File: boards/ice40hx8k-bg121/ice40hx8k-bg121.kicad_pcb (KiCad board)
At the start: 4 copper layers, 22.9 x 48.3 mm, 51 parts, among them J1 BANK 0, J2 BANK 1, J3 BANK 2, J4 BANK 3, U1 AP7361C-33Y5-13, U2 AP7361C-12Y5-13, U3 iCE40HX8K-BG121(121-Ball_caBG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, U4 LE25U20AMB, U5 ASDMB-xxxMHz

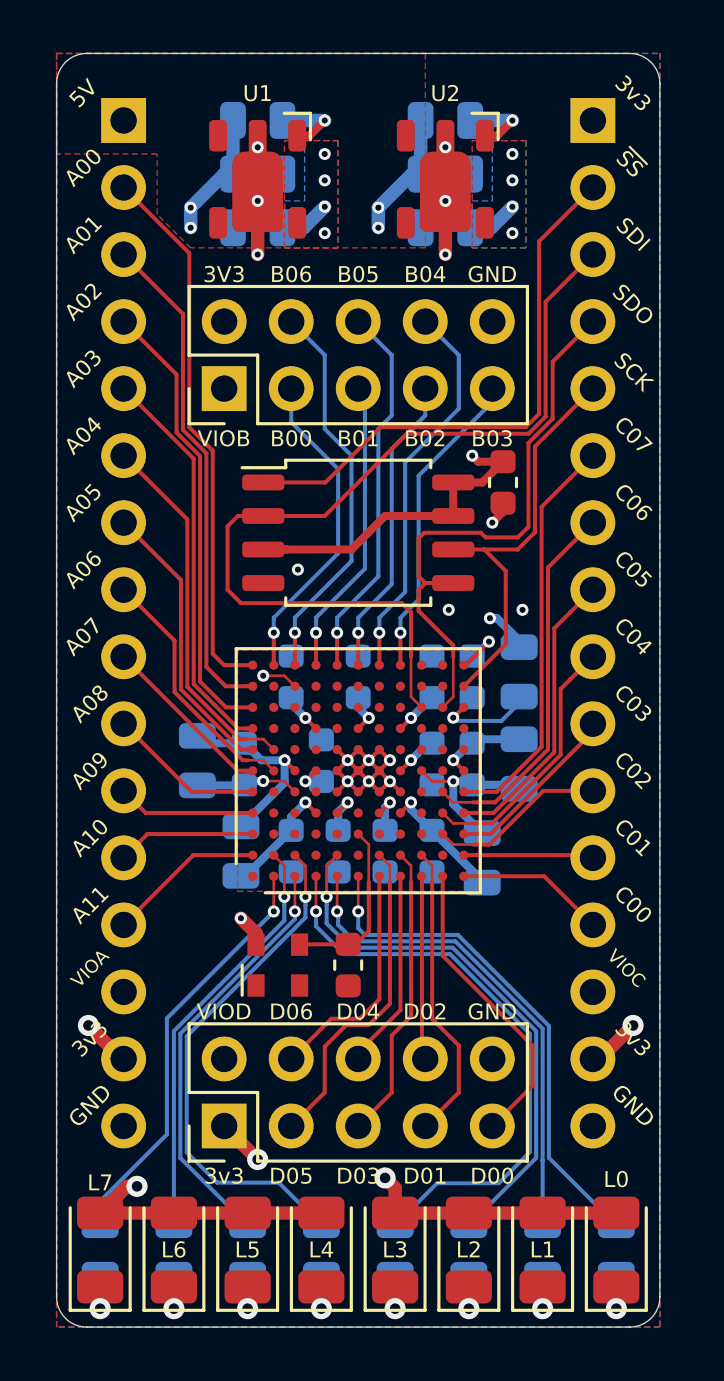
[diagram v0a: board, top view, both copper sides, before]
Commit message: Fixed errors in main README. Added boards.
Accidentally committed changes to ice40hx8k-bg121 and atsamd21e18a
boards.

The ice40hx8k-bg121 changes include adding access to CBSEL0/1 and
rerouting IO.

The atsamd21e18a changes include rerouting IO to prioritize USB
D+/- routing.
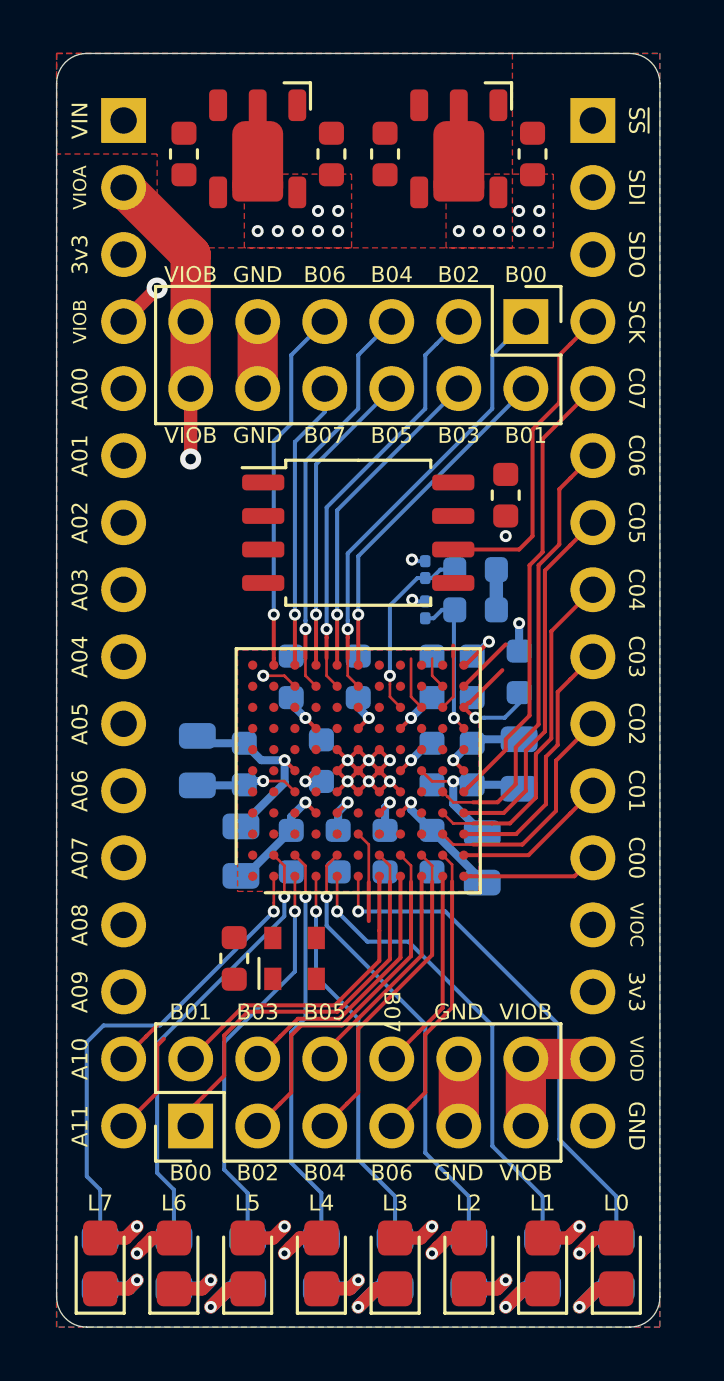
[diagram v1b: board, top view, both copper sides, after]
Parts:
- removed C20: 22p, Capacitor_SMD:C_0603_1608Metric
- removed REF**: OSHW-Symbol_6.7x6mm_SilkScreen, Symbol:OSHW-Symbol_6.7x6mm_SilkScreen
- added C21: 0.1u, Capacitor_SMD:C_0603_1608Metric, F.Cu at (27.1, 49.5)
- added JP1: CBSEL1, Resistor_SMD:R_0201_0603Metric, B.Cu at (34.3, 36.3)
- added JP2: CBSEL0, Resistor_SMD:R_0201_0603Metric, B.Cu at (34.3, 34.8)
- C1, C2, C3, C4: footprint Capacitor_SMD:C_0805_2012Metric -> Capacitor_SMD:C_0603_1608Metric; moved to F.Cu
- D10, D3, D4, D5, D6, D7, D8, D9: footprint LED_SMD:LED_1206_3216Metric -> LED_SMD:LED_0805_2012Metric_Castellated
- J1: value BANK 0 -> Conn_01x16
- J2: value BANK 1 -> Conn_01x16
- J3: value BANK 2 -> Conn_02x06_Odd_Even; footprint Connector_PinHeader_2.54mm:PinHeader_2x05_P2.54mm_Vertical -> Connector_PinHeader_2.54mm:PinHeader_2x06_P2.54mm_Vertical
- J4: value BANK 3 -> Conn_02x06_Odd_Even; footprint Connector_PinHeader_2.54mm:PinHeader_2x05_P2.54mm_Vertical -> Connector_PinHeader_2.54mm:PinHeader_2x06_P2.54mm_Vertical
- R1, R12, R2: footprint Resistor_SMD:R_0805_2012Metric -> Resistor_SMD:R_0603_1608Metric
- moved R1 20.3 mm to (36.2, 36.3)
- moved R2 17.1 mm to (36.2, 34.8)
- moved J4 11.7 mm to (38.1, 25.4), turned to 270 degrees
- moved C4 4.33 mm to (38.4, 19.1), turned to 90 degrees
- moved C2 3.95 mm to (30.7, 19.1), turned to 90 degrees
- moved C1 2.90 mm to (25.1, 19.1), turned to 90 degrees
- moved C3 2.41 mm to (32.8, 19.1), turned to 90 degrees
- moved J3 1.27 mm to (25.4, 55.9)
- moved U2 1.26 mm to (35.6, 18.9)
- moved U1 1.15 mm to (27.9, 18.9)
- moved U5 0.68 mm to (29.3, 49.5)
- moved D10 0.51 mm to (41.5, 61.1)
- moved D3 0.51 mm to (22.0, 61.1)
- moved D4 0.51 mm to (24.8, 61.1)
- moved D5 0.51 mm to (27.6, 61.1)
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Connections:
- net Net-(U3-PadK8) renamed CDONE
- C19 pad 2: VCCIO_C -> +3V3
- J1 pad 10: IO_A08 -> IO_A05
- J1 pad 11: IO_A09 -> IO_A06
- J1 pad 12: IO_A10 -> IO_A07
- J1 pad 13: IO_A11 -> IO_A08
- J1 pad 14: VCCIO_A -> IO_A09
- J1 pad 15: +3V3 -> IO_A10
- J1 pad 16: GND -> IO_A11
- J1 pad 2: IO_A00 -> VCCIO_B
- J1 pad 3: IO_A01 -> +3V3
- J1 pad 4: IO_A02 -> VCCIO_A
- J1 pad 5: IO_A03 -> IO_A00
- J1 pad 6: IO_A04 -> IO_A01
- J1 pad 7: IO_A05 -> IO_A02
- J1 pad 8: IO_A06 -> IO_A03
- J1 pad 9: IO_A07 -> IO_A04
- J2 pad 1: +3V3 -> PROG_SS_B
- J2 pad 10: IO_C03 -> IO_C02
- J2 pad 11: IO_C02 -> IO_C01
- J2 pad 12: IO_C01 -> IO_C00
- J2 pad 13: IO_C00 -> VCCIO_C
- J2 pad 14: VCCIO_C -> +3V3
- J2 pad 15: +3V3 -> VCCIO_D
- J2 pad 2: PROG_SS_B -> PROG_SDI
- J2 pad 3: PROG_SDI -> PROG_SDO
- J2 pad 4: PROG_SDO -> PROG_SCK
- J2 pad 5: PROG_SCK -> IO_C07
- J2 pad 6: IO_C07 -> IO_C06
- J2 pad 7: IO_C06 -> IO_C05
- J2 pad 8: IO_C05 -> IO_C04
- J2 pad 9: IO_C04 -> IO_C03
- J3 pad 1: +3V3 -> IO_D00
- J3 pad 2: VCCIO_D -> IO_D01
- J3 pad 3: IO_D05 -> IO_D02
- J3 pad 4: IO_D06 -> IO_D03
- J3 pad 5: IO_D03 -> IO_D04
- J3 pad 6: IO_D04 -> IO_D05
- J3 pad 7: IO_D01 -> IO_D06
- J3 pad 8: IO_D02 -> IO_D07
- J3 pad 9: IO_D00 -> GND
- J4 pad 1: VCCIO_B -> IO_B00
- J4 pad 2: +3V3 -> IO_B01
- J4 pad 3: IO_B00 -> IO_B02
- J4 pad 4: IO_B06 -> IO_B03
- J4 pad 5: IO_B01 -> IO_B04
- J4 pad 7: IO_B02 -> IO_B06
- J4 pad 8: IO_B04 -> IO_B07
- J4 pad 9: IO_B03 -> GND
- R1 pad 1: +5V -> CBSEL0
- R1 pad 2: Net-(R1-Pad2) -> GND
- R2 pad 1: +5V -> CBSEL1
- R2 pad 2: Net-(R2-Pad2) -> GND
- U1 pad 1: Net-(R1-Pad2) -> +5V
- U2 pad 1: Net-(R2-Pad2) -> +5V
- U3 pad A2: IO_A11 -> Net-(U3-PadA2)
- U3 pad A3: IO_A10 -> Net-(U3-PadA3)
- U3 pad A4: IO_A09 -> IO_A10
- U3 pad B11: IO_B00 -> IO_B06
- U3 pad B4: Net-(U3-PadB4) -> IO_A11
- U3 pad B5: Net-(U3-PadB5) -> IO_A09
- U3 pad C11: IO_B06 -> IO_B07
- U3 pad D10: Net-(U3-PadD10) -> IO_B04
- U3 pad D11: IO_B01 -> IO_B05
- U3 pad E10: Net-(U3-PadE10) -> IO_B02
- U3 pad E11: IO_B05 -> IO_B03
- U3 pad F10: Net-(U3-PadF10) -> IO_B00
- U3 pad F11: IO_B02 -> IO_B01
- U3 pad G1: IO_D06 -> IO_D01
- U3 pad G11: IO_B04 -> Net-(U3-PadG11)
- U3 pad G2: IO_D05 -> IO_D00
- U3 pad H1: IO_D04 -> IO_D03
- U3 pad H11: IO_B03 -> Net-(U3-PadH11)
- U3 pad H2: IO_D03 -> IO_D02
- U3 pad J1: IO_D02 -> IO_D05
- U3 pad J2: IO_D01 -> IO_D04
- U3 pad K1: IO_D00 -> IO_D07
- U3 pad K10: Net-(U3-PadK10) -> PROG_SS_B
- U3 pad K2: Net-(U3-PadK2) -> IO_D06
- U4 pad 3: VCCIO_C -> +3V3
- U4 pad 7: VCCIO_C -> +3V3
- U4 pad 8: VCCIO_C -> +3V3
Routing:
- net PROG_SDI: track 34.1 -> 2.01 mm
- net VCCIO_C: track 42.6 -> 19.4 mm, vias 3 -> 2
- net IO_A00: track 20.8 -> 0.00 mm
- net PROG_SS_B: track 21.0 -> 1.21 mm
- net PROG_SDO: track 21.7 -> 2.51 mm
- net IO_A01: track 19.0 -> 0.00 mm
- net IO_A02: track 17.2 -> 0.00 mm
- net IO_A03: track 15.2 -> 0.10 mm
- net IO_A04: track 14.0 -> 0.00 mm
- net VCCIO_A: track 12.3 -> 25.4 mm, vias 1 -> 2
- net IO_B07: track 0.00 -> 10.9 mm, vias 0 -> 1
- net IO_A05: track 10.9 -> 0.00 mm
- net +5V: track 9.85 -> 0.00 mm, vias 4 -> 0
- net IO_A06: track 9.77 -> 0.00 mm
- net VCCIO_B: track 19.2 -> 28.4 mm, vias 1 -> 2
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- removed copper zone on B.Cu, net +1V2
- removed copper zone on B.Cu, net +3V3
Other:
- board text added: "B07"
- board text added: "CBSEL0"
- board text added: "CBSEL1"
- board text added: "VIN"
- board text removed: "3V3"
- board text removed: "5V"
- board text removed: "D00"
- board text removed: "D01"
- board text removed: "D02"
- board text removed: "D03"
- board text removed: "D04"
- board text removed: "D05"
- board text removed: "D06"

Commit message: Added FT2232H breakout for programming /boards/ice40hx8k-bg121/
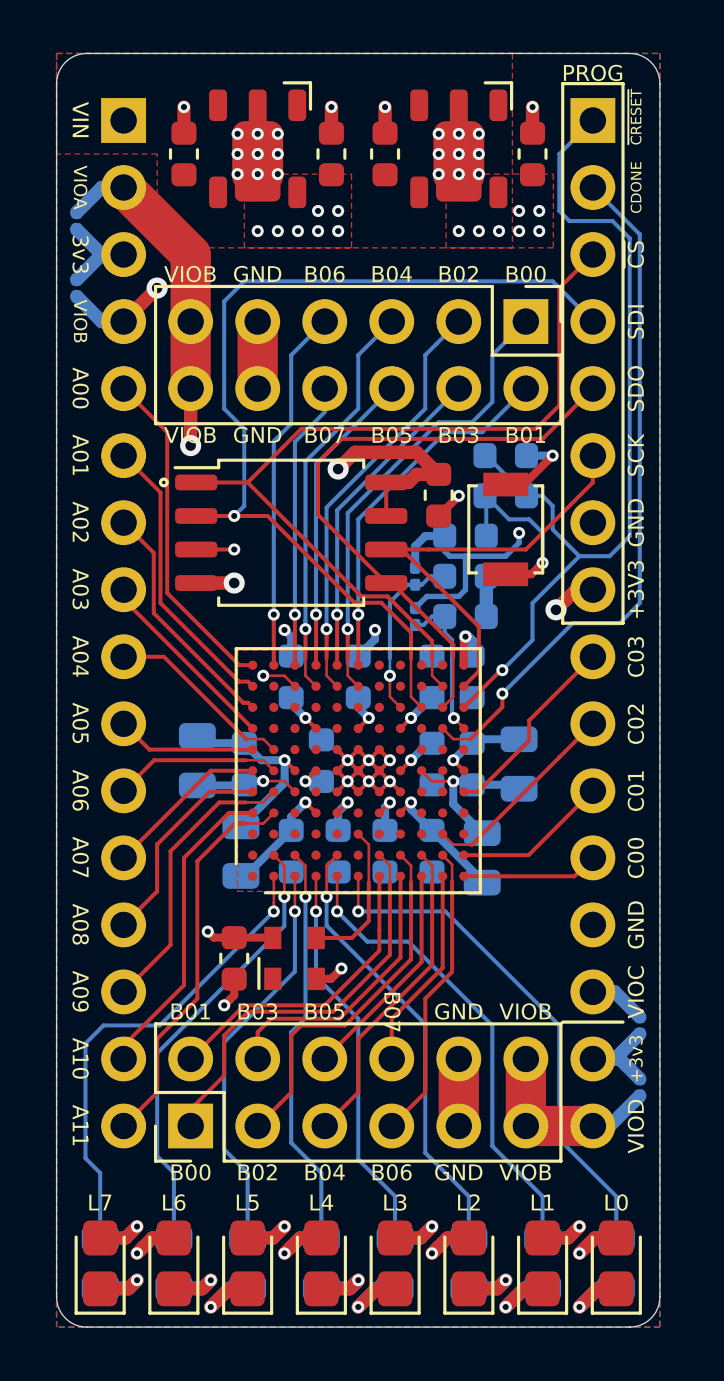
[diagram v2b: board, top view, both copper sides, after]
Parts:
- added C20: 0.1u, Capacitor_SMD:C_0603_1608Metric, B.Cu at (37.3, 30.5)
- added JP3: VCCIO_A, jkiv-library:J_NO_0201_0603Metric, B.Cu at (21.1, 24.1)
- added JP4: VCCIO_B, jkiv-library:J_NO_0201_0603Metric, B.Cu at (21.1, 21.6)
- added JP5: VCCIO_C, jkiv-library:J_NO_0201_0603Metric, B.Cu at (42.4, 52.1)
- added JP6: VCCIO_D, jkiv-library:J_NO_0201_0603Metric, B.Cu at (42.4, 54.4)
- added R14: 10k, Resistor_SMD:R_0603_1608Metric, B.Cu at (35.8, 33.5)
- added REF**: OSHW-Symbol_6.7x6mm_SilkScreen, Symbol:OSHW-Symbol_6.7x6mm_SilkScreen, B.Cu at (32.0, 19.8)
- added SW1: B3U-1000P, Button_Switch_SMD:SW_SPST_B3U-1000P, F.Cu at (37.3, 33.3)
- JP1, JP2: footprint Resistor_SMD:R_0201_0603Metric -> jkiv-library:J_NO_0201_0603Metric
- moved R12 6.69 mm to (37.3, 32.0), turned to 0 degrees
- moved C19 2.54 mm to (34.8, 32.0)
- moved U4 2.54 mm to (29.2, 33.4)
- moved JP1 0.46 mm to (33.9, 36.6)
- moved JP2 0.46 mm to (33.9, 35.1)
- moved R1 0.46 mm to (35.8, 36.6)
- moved R2 0.46 mm to (35.8, 35.1)
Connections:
- J2 pad 1: PROG_SS_B -> PROG_CRESET_B
- J2 pad 13: VCCIO_C -> GND
- J2 pad 14: +3V3 -> VCCIO_C
- J2 pad 15: VCCIO_D -> +3V3
- J2 pad 16: GND -> VCCIO_D
- J2 pad 2: PROG_SDI -> CDONE
- J2 pad 3: PROG_SDO -> PROG_SS_B
- J2 pad 4: PROG_SCK -> PROG_SDI
- J2 pad 5: IO_C07 -> PROG_SDO
- J2 pad 6: IO_C06 -> PROG_SCK
- J2 pad 7: IO_C05 -> GND
- J2 pad 8: IO_C04 -> +3V3
- R12 pad 1: VCCIO_C -> Net-(R12-Pad1)
- U3 pad K4: IO_C04 -> Net-(U3-PadK4)
- U3 pad K5: IO_C06 -> Net-(U3-PadK5)
- U3 pad L3: IO_C03 -> Net-(U3-PadL3)
- U3 pad L4: IO_C05 -> Net-(U3-PadL4)
- U3 pad L5: IO_C07 -> IO_C03
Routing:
- net PROG_SDI: track 2.01 -> 36.5 mm, vias 0 -> 1
- net PROG_SS_B: track 1.21 -> 32.6 mm
- net PROG_CRESET_B: track 4.90 -> 33.8 mm
- net CDONE: track 0.00 -> 26.6 mm, vias 0 -> 1
- net +3V3: track 25.7 -> 47.1 mm, vias 19 -> 22
- net PROG_SDO: track 2.51 -> 23.3 mm
- net GND: track 18.5 -> 36.2 mm, vias 7 -> 35
- net IO_C07: track 17.3 -> 0.00 mm
- net IO_C06: track 16.9 -> 0.00 mm
- net IO_C05: track 13.9 -> 0.00 mm
- net IO_C04: track 12.9 -> 0.00 mm
- net IO_A00: track 0.00 -> 12.8 mm
- net IO_A01: track 0.00 -> 11.0 mm
- net IO_A09: track 0.00 -> 10.9 mm
- net IO_A11: track 3.93 -> 14.8 mm
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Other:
- board text added: "+3V3"
- board text added: "+3v3"
- board text added: "CDONE"
- board text added: "PROG"
- board text added: "~CRESET"
- board text added: "~CS"
- board text removed: "C04"
- board text removed: "C05"
- board text removed: "C06"
- board text removed: "C07"
- board text removed: "~SS"

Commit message: Changes to ice40hx8k-bg121 PCB. (Unsure.)
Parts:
- moved REF** 0.36 mm to (31.8, 19.6)
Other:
- board text added: "fourside.io"
- board text added: "ice40hx8k breakout 2020-03"
- board text removed: "ice40hx8k breakout 2020-03 fourside.io"
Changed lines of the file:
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@@
   (general
     (thickness 1.6)
-    (drawings 90)
+    (drawings 91)
     (tracks 711)
     (zones 0)
@@
   )
   (setup
-    (last_trace_width 0.508)
+    (last_trace_width 0.25)
     (user_trace_width 0.1016)
     (user_trace_width 0.1524)
@@
     (visible_elements 7FFFFFFF)
     (pcbplotparams
-      (layerselection 0x0100c_7ffffff8)
+      (layerselection 0x010fc_ffffffff)
       (usegerberextensions true)
       (usegerberattributes false)
@@
       (creategerberjobfile false)
       (excludeedgelayer true)
-      (linewidth 0.150000)
+      (linewidth 0.100000)
       (plotframeref false)
       (viasonmask false)
@@
   )
   (module Symbol:OSHW-Symbol_6.7x6mm_SilkScreen (layer B.Cu)
-    (at 32.004 19.812 180)
+    (at 31.75 19.558 180)
     (descr "Open Source Hardware Symbol")
     (tags "Logo Symbol OSHW")
@@
     )
   )
+  (gr_text fourside.io (at 31.75 58.039) (layer B.SilkS)
+    (effects (font (size 0.8 0.8) (thickness 0.1)) (justify mirror))
+  )
   (gr_line (start 39.497 51.943) (end 41.783 51.943) (layer F.SilkS) (width 0.12))
   (gr_text VIOB (at 21.0185 20.066 270) (layer B.SilkS)
@@
     (effects (font (size 0.6 0.6) (thickness 0.1)))
   )
-  (gr_text B07 (at 33.02 51.562 270) (layer F.SilkS)
+  (gr_text B07 (at 33.02 51.562) (layer F.SilkS)
     (effects (font (size 0.6 0.6) (thickness 0.1)))
   )
@@
     (effects (font (size 0.4 0.4) (thickness 0.1)) (justify mirror))
   )
-  (gr_text "ice40hx8k breakout\n2020-03\nfourside.io" (at 31.496 49.53) (layer B.SilkS)
+  (gr_text "ice40hx8k breakout\n2020-03" (at 31.623 50.546) (layer B.SilkS)
     (effects (font (size 0.8 0.8) (thickness 0.1)) (justify mirror))
   )

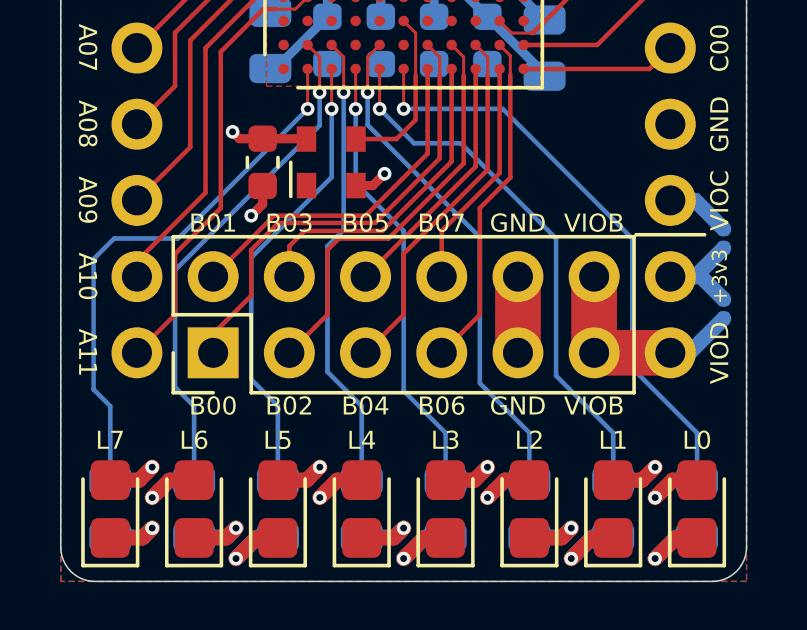
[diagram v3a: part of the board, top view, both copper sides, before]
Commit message: Fixed typo on IO Bank D's silkscreen.
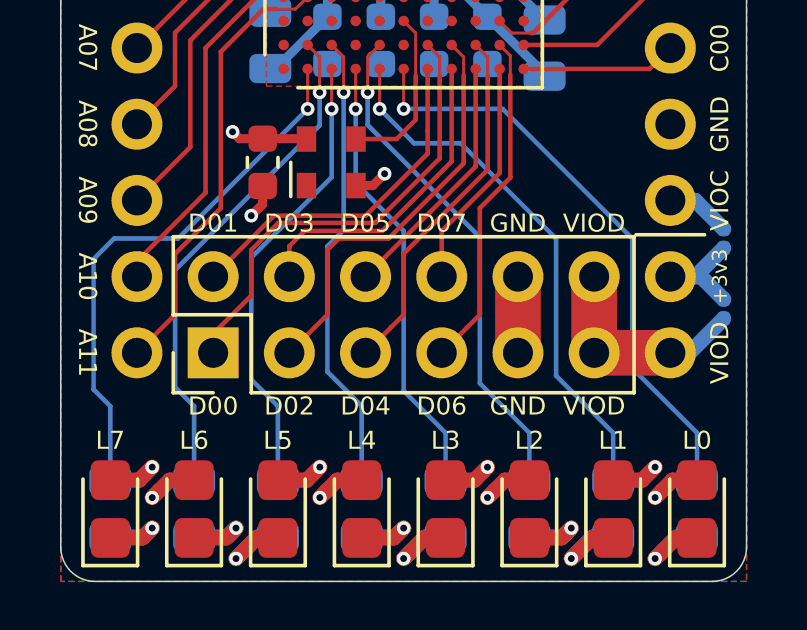
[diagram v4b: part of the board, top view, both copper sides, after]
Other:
- board text added: "D00"
- board text added: "D01"
- board text added: "D02"
- board text added: "D03"
- board text added: "D04"
- board text added: "D05"
- board text added: "D06"
- board text added: "D07"
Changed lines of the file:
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@@
   )
   (gr_circle (center 24.384 31.496) (end 24.257 31.496) (layer F.SilkS) (width 0.12))
-  (gr_text B05 (at 30.480001 51.562) (layer F.SilkS)
+  (gr_text D05 (at 30.480001 51.562) (layer F.SilkS)
     (effects (font (size 0.6 0.6) (thickness 0.1)))
   )
-  (gr_text B04 (at 30.48 57.657999) (layer F.SilkS)
+  (gr_text D04 (at 30.48 57.657999) (layer F.SilkS)
     (effects (font (size 0.6 0.6) (thickness 0.1)))
   )
-  (gr_text B02 (at 27.94 57.658) (layer F.SilkS)
+  (gr_text D02 (at 27.94 57.658) (layer F.SilkS)
     (effects (font (size 0.6 0.6) (thickness 0.1)))
   )
-  (gr_text VIOB (at 38.1 57.658) (layer F.SilkS)
+  (gr_text VIOD (at 38.1 57.658) (layer F.SilkS)
     (effects (font (size 0.6 0.6) (thickness 0.1)))
   )
-  (gr_text B00 (at 25.4 57.658) (layer F.SilkS)
+  (gr_text D00 (at 25.4 57.658) (layer F.SilkS)
     (effects (font (size 0.6 0.6) (thickness 0.1)))
   )
-  (gr_text B01 (at 25.4 51.562) (layer F.SilkS)
+  (gr_text D01 (at 25.4 51.562) (layer F.SilkS)
     (effects (font (size 0.6 0.6) (thickness 0.1)))
   )
-  (gr_text B06 (at 33.02 57.658) (layer F.SilkS)
+  (gr_text D06 (at 33.02 57.658) (layer F.SilkS)
     (effects (font (size 0.6 0.6) (thickness 0.1)))
   )
@@
     (effects (font (size 0.6 0.6) (thickness 0.1)))
   )
-  (gr_text B03 (at 27.94 51.562) (layer F.SilkS)
+  (gr_text D03 (at 27.94 51.562) (layer F.SilkS)
     (effects (font (size 0.6 0.6) (thickness 0.1)))
   )
-  (gr_text VIOB (at 38.1 51.562) (layer F.SilkS)
+  (gr_text VIOD (at 38.1 51.562) (layer F.SilkS)
     (effects (font (size 0.6 0.6) (thickness 0.1)))
   )
-  (gr_text B07 (at 33.02 51.562) (layer F.SilkS)
+  (gr_text D07 (at 33.02 51.562) (layer F.SilkS)
     (effects (font (size 0.6 0.6) (thickness 0.1)))
   )

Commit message: Updated version info on backside of board.
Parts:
- removed JP3: VCCIO_A, jkiv-library:J_NO_0201_0603Metric
- removed JP4: VCCIO_B, jkiv-library:J_NO_0201_0603Metric
- removed JP5: VCCIO_C, jkiv-library:J_NO_0201_0603Metric
- removed JP6: VCCIO_D, jkiv-library:J_NO_0201_0603Metric
- moved JP1 2.39 mm to (33.7, 34.2)
- moved JP2 1.40 mm to (32.8, 34.2), turned to 90 degrees
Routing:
- net +3V3: track 47.1 -> 36.1 mm
- net CBSEL0: track 5.84 -> 9.55 mm
- net CBSEL1: track 6.63 -> 9.35 mm
- net VCCIO_D: track 25.5 -> 23.3 mm
- net VCCIO_C: track 18.1 -> 15.9 mm
- net VCCIO_B: track 30.4 -> 28.3 mm
- net VCCIO_A: track 27.5 -> 25.4 mm
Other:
- board text added: "(cc) fourside.io"
- board text added: "ice40hx8k breakout 2020-04"
- board text removed: "fourside.io"
- board text removed: "ice40hx8k breakout 2020-03"
